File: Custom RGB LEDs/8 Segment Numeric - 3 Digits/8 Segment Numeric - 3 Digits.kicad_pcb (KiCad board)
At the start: 4 copper layers, 81.3 x 24.1 mm, 38 parts

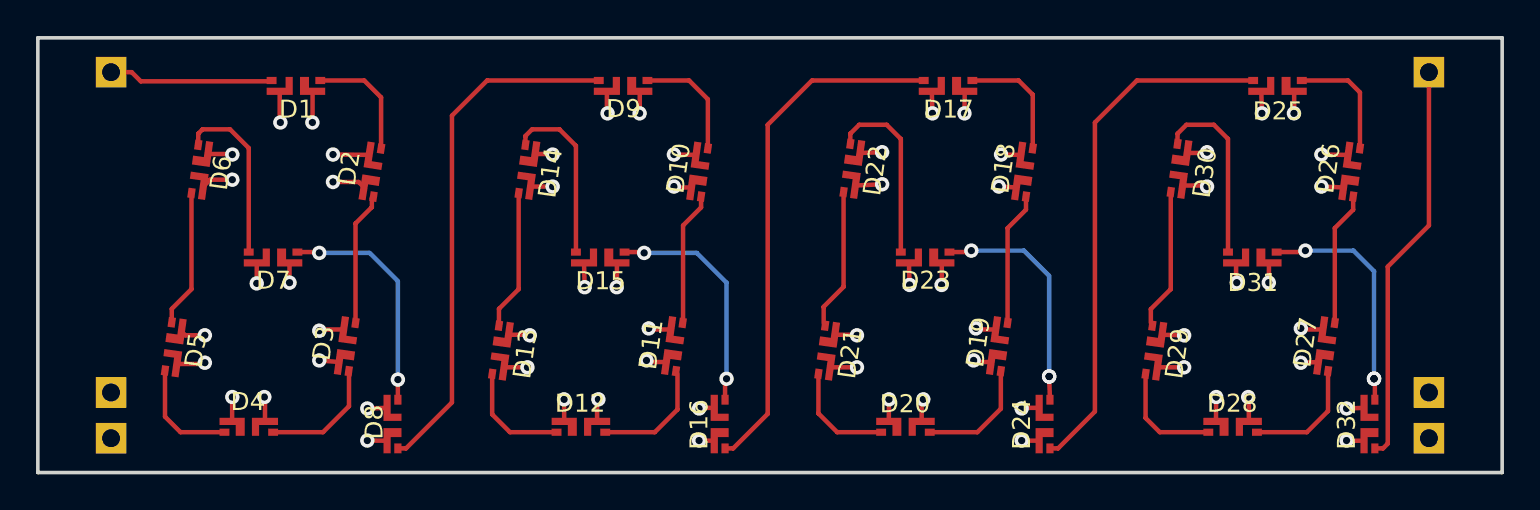
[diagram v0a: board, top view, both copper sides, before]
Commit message: Season 1/2 Speedo board updates
Season 1/2 Speedo board mostly complete, a few modifications still pending.
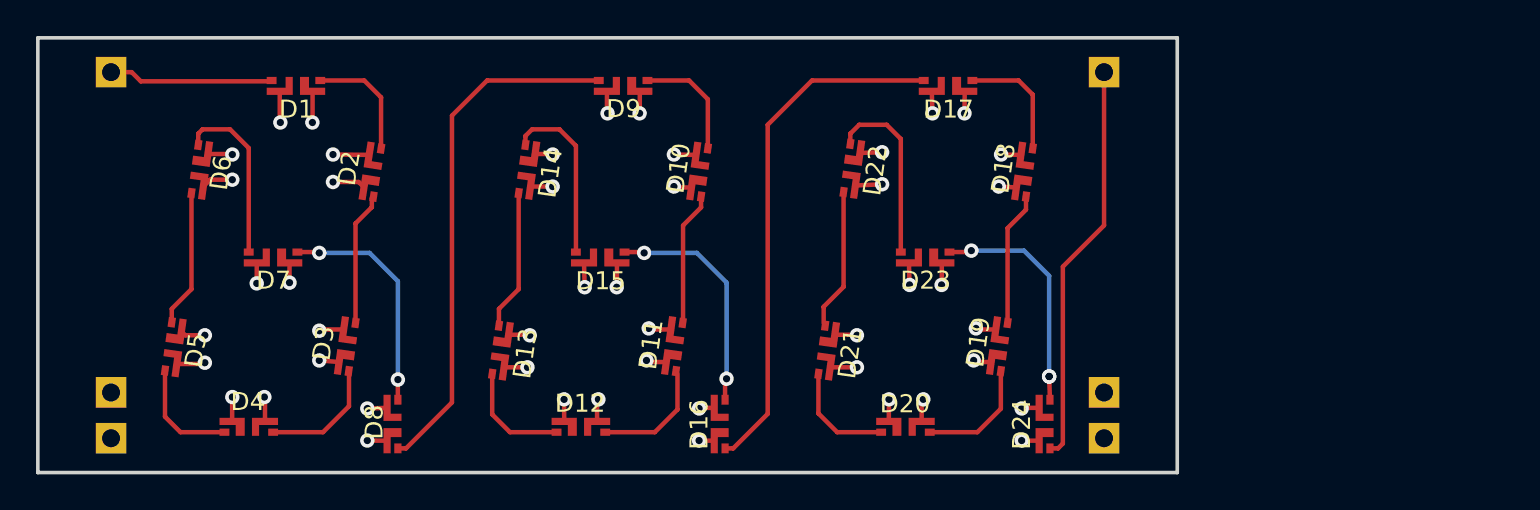
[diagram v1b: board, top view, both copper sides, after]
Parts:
- removed D25, D26, D27, D28, D29, D30, D31, D32: SK6812-EC3210F, Custom Footprint Library:SK6812-EC3210F
- moved ? 18.0 mm to (139.2, 84.7)
- moved ? 18.0 mm to (139.2, 66.9)
- moved ? 18.0 mm to (139.2, 87.2)
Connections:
- ? pad 1: unconnected-(D32-DOUT-Pad2) -> Net-(D24-DOUT)
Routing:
- net unconnected-(D32-DOUT-Pad2): track 22.4 -> 0.00 mm
- net Net-(D31-DOUT): track 13.1 -> 0.00 mm, vias 3 -> 0
- net +5V: track 42.8 -> 32.4 mm, vias 32 -> 24
- net Net-(D30-DOUT): track 10.2 -> 0.00 mm
- net GND: track 39.0 -> 29.6 mm, vias 32 -> 24
- net Net-(D29-DOUT): track 7.72 -> 0.00 mm
- net Net-(D26-DOUT): track 7.44 -> 0.00 mm
- net Net-(D24-DOUT): track 29.1 -> 22.4 mm
- net Net-(D27-DOUT): track 6.65 -> 0.00 mm
- net Net-(D25-DOUT): track 6.61 -> 0.00 mm
- net Net-(D28-DOUT): track 6.26 -> 0.00 mm
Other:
- board size 81.3 x 24.1 mm -> 63.2 x 24.1 mm
